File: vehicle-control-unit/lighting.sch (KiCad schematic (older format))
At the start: 23 parts, among them J12 Conn_01x06_Male, Q1 BC517, U3 ULN2803A

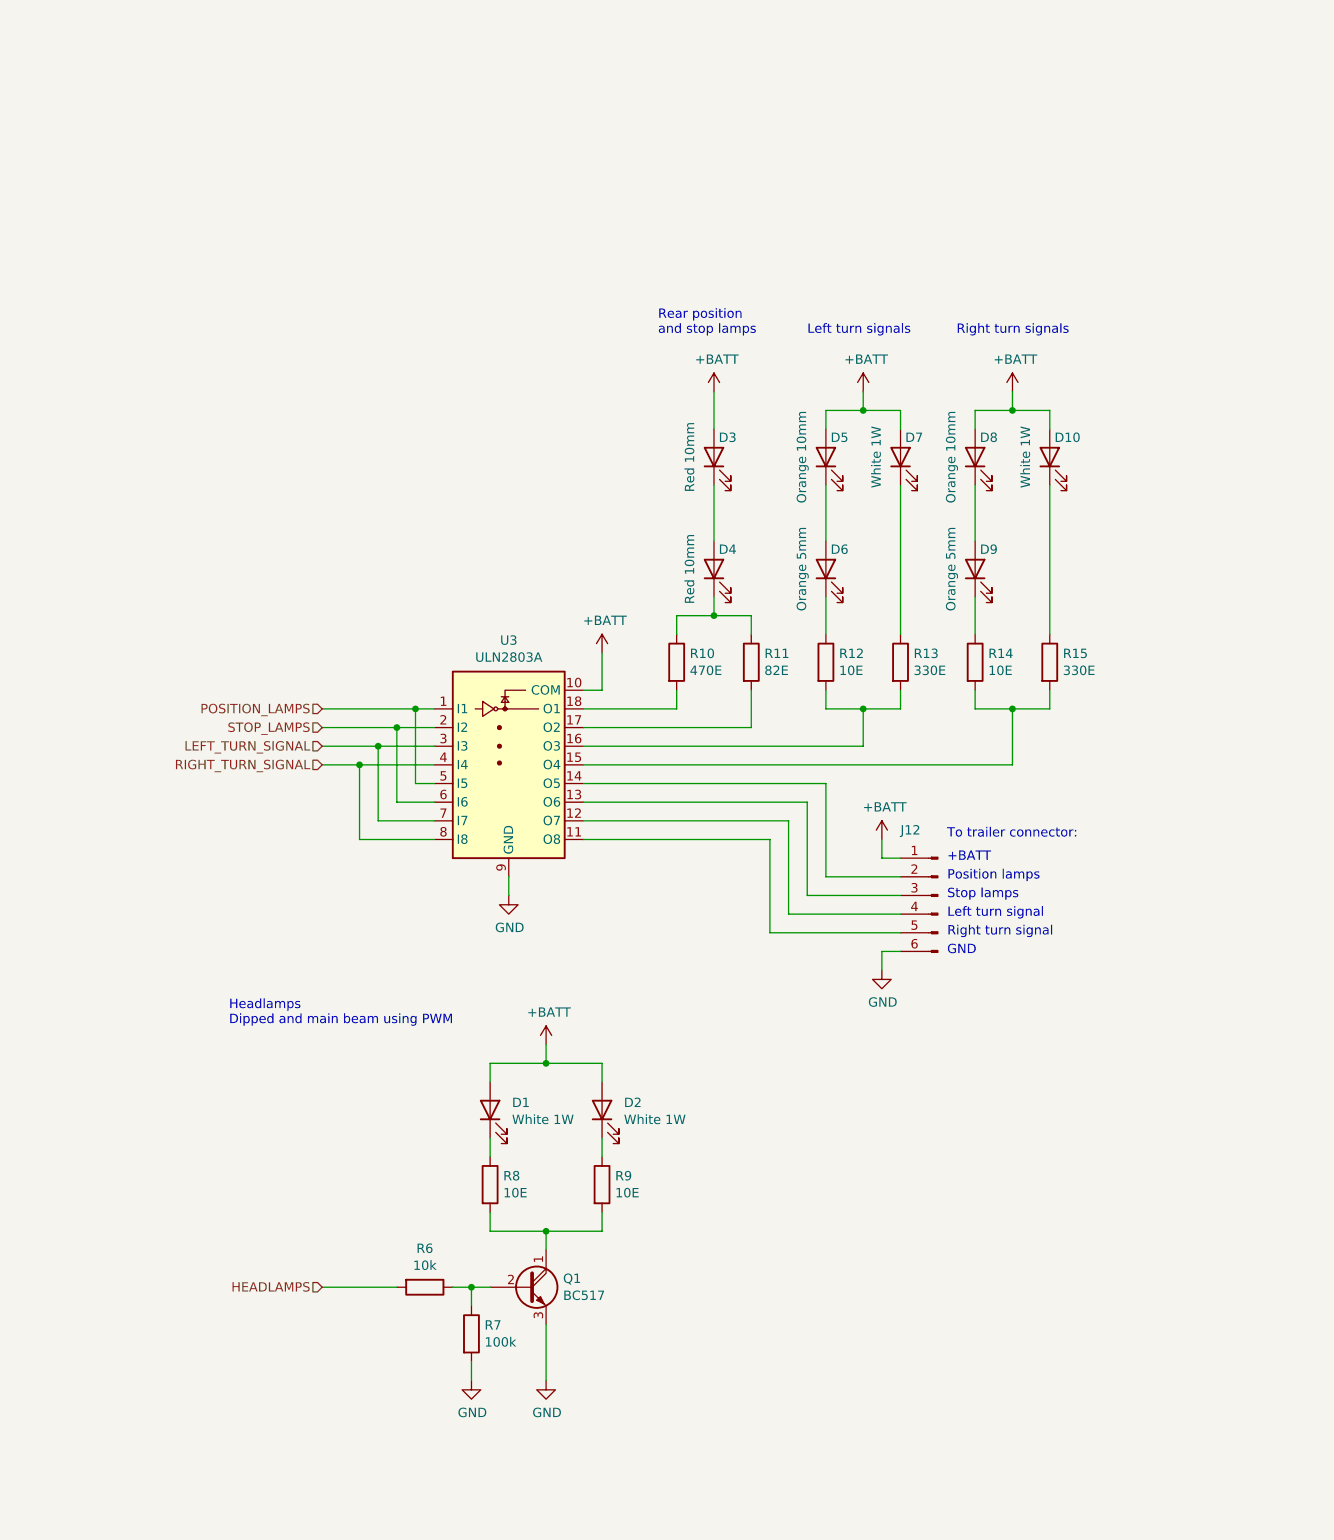
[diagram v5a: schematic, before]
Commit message: Wire all turn signal LEDs in parallel
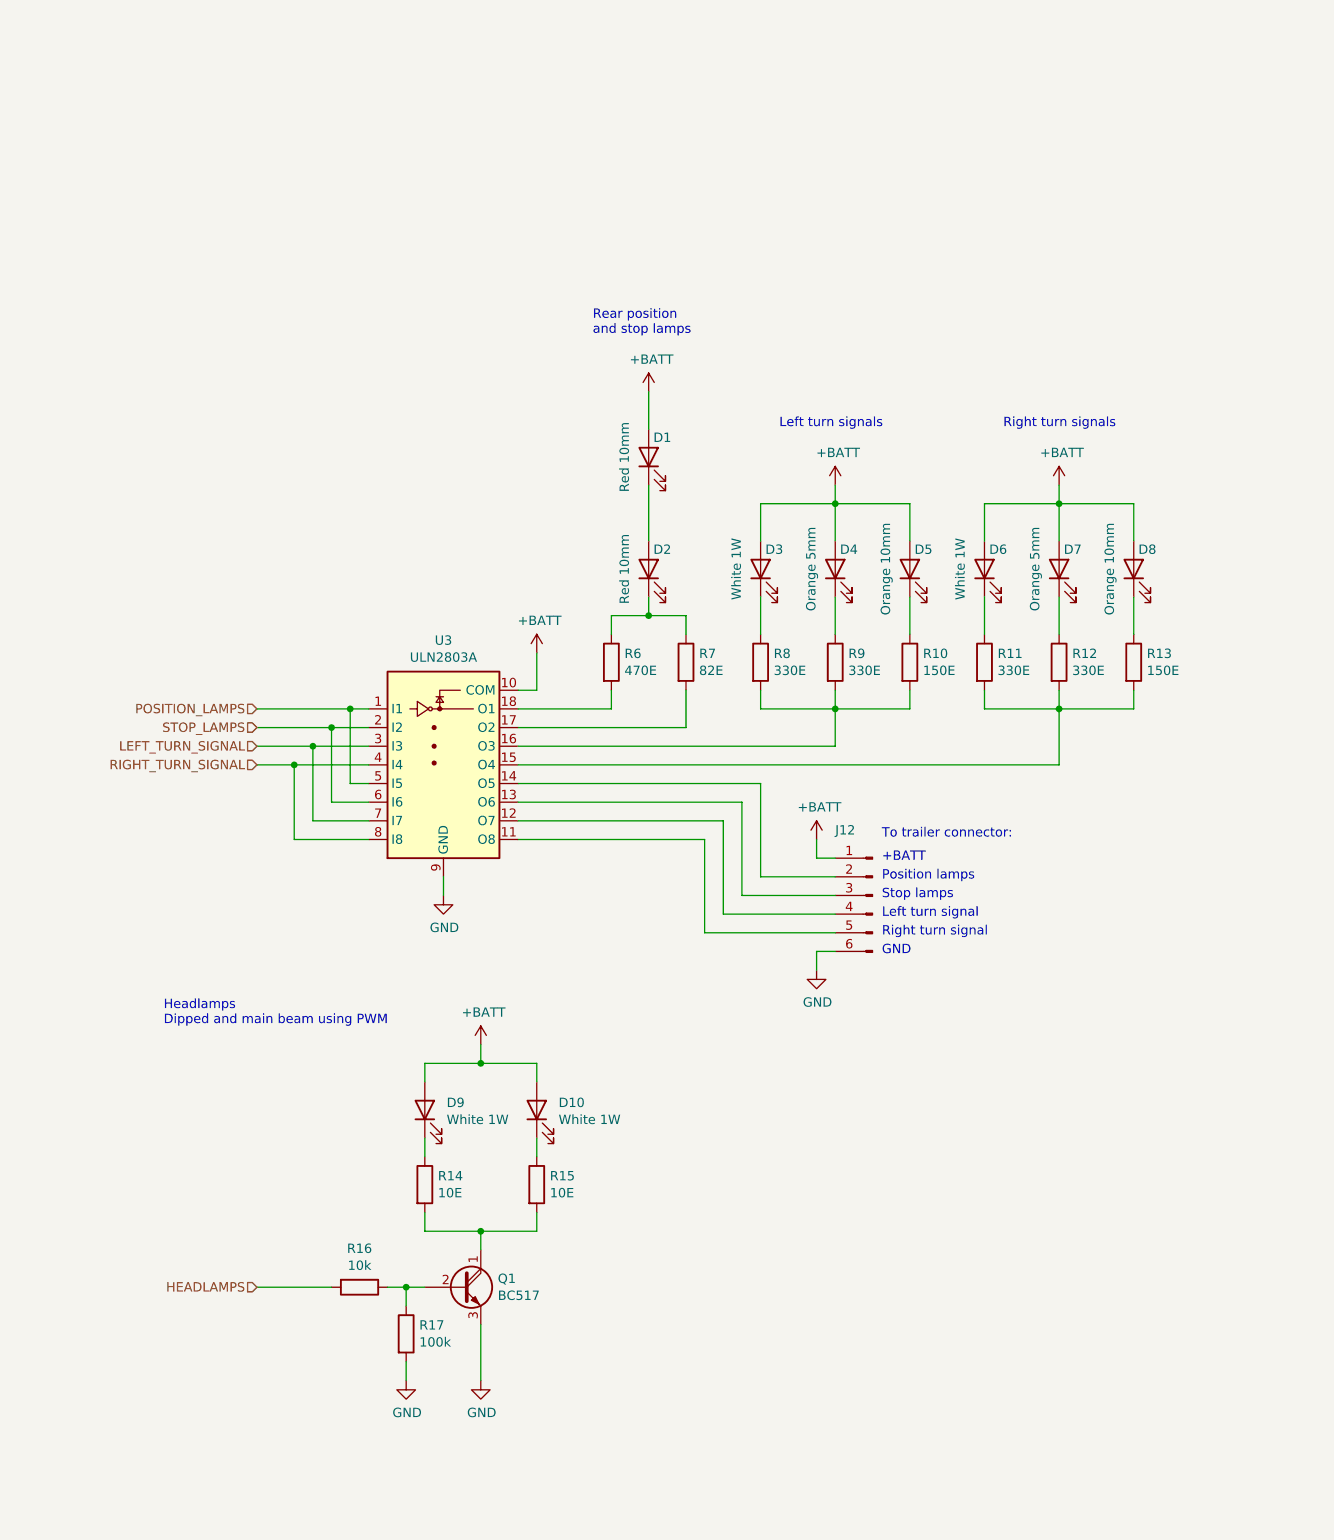
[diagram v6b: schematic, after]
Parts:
- added R10, R13: 150E, symbol Device:R
- R11: renamed from R14; value 10E -> 330E
- R8: renamed from R12; value 10E -> 330E
- renumbered D3 to D1, D2 to D10, D4 to D2, D7 to D3, D6 to D4, D10 to D6, D9 to D7, D1 to D9, R15 to R12, R8 to R14, R9 to R15, R6 to R16, R7 to R17, R10 to R6, R11 to R7, R13 to R9
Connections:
- net +BATT: now also D4.2 (A), D7.2 (A)
- net at R11.2, R12.2, U3.15 (O4): now also R13.2
- net at R8.2, R9.2, U3.16 (O3): now also R10.2
- net at D5.1 (K): now also R10.1; no longer D4.2 (A)
- net at D4.1 (K): now also R9.1; no longer R8.1
- net at D3.1 (K): now also R8.1; no longer R9.1
- net at D8.1 (K): now also R13.1; no longer D7.2 (A)
- net at D7.1 (K): now also R12.1; no longer R11.1
- net at D6.1 (K): now also R11.1; no longer R12.1
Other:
- moved on the sheet: D1, D10, D2, D3, D4, D5, D6, D7, D8, D9, J12, Q1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

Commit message: Assign footprints
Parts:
- D1, D10, D2, D3, D4, D5, D6, D7, D8, D9: footprint (none) -> Connector_PinHeader_2.54mm:PinHeader_1x02_P2.54mm_Horizontal
- J12: footprint (none) -> Connector_PinHeader_2.54mm:PinHeader_1x06_P2.54mm_Horizontal
- R10, R11, R12, R13, R14, R15, R16, R17, R6, R7, R8, R9: footprint (none) -> Resistor_THT:R_Axial_DIN0207_L6.3mm_D2.5mm_P10.16mm_Horizontal
- U3: footprint (none) -> Package_DIP:DIP-18_W7.62mm
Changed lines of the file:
@@
 F 0 "R17" H 3120 8746 50  0000 L CNN
 F 1 "100k" H 3120 8655 50  0000 L CNN
-F 2 "" V 2980 8700 50  0001 C CNN
+F 2 "Resistor_THT:R_Axial_DIN0207_L6.3mm_D2.5mm_P10.16mm_Horizontal" V 2980 8700 50  0001 C CNN
 F 3 "~" H 3050 8700 50  0001 C CNN
 	1    3050 8700
@@
 F 0 "R16" V 2593 8450 50  0000 C CNN
 F 1 "10k" V 2684 8450 50  0000 C CNN
-F 2 "" V 2730 8450 50  0001 C CNN
+F 2 "Resistor_THT:R_Axial_DIN0207_L6.3mm_D2.5mm_P10.16mm_Horizontal" V 2730 8450 50  0001 C CNN
 F 3 "~" H 2800 8450 50  0001 C CNN
 	1    2800 8450
@@
 F 0 "R14" H 3220 7946 50  0000 L CNN
 F 1 "10E" H 3220 7855 50  0000 L CNN
-F 2 "" V 3080 7900 50  0001 C CNN
+F 2 "Resistor_THT:R_Axial_DIN0207_L6.3mm_D2.5mm_P10.16mm_Horizontal" V 3080 7900 50  0001 C CNN
 F 3 "~" H 3150 7900 50  0001 C CNN
 	1    3150 7900
@@
 F 0 "R15" H 3820 7946 50  0000 L CNN
 F 1 "10E" H 3820 7855 50  0000 L CNN
-F 2 "" V 3680 7900 50  0001 C CNN
+F 2 "Resistor_THT:R_Axial_DIN0207_L6.3mm_D2.5mm_P10.16mm_Horizontal" V 3680 7900 50  0001 C CNN
 F 3 "~" H 3750 7900 50  0001 C CNN
 	1    3750 7900
@@
 F 0 "D9" V 3189 7383 50  0000 R CNN
 F 1 "White 1W" V 3098 7383 50  0000 R CNN
-F 2 "" H 3150 7500 50  0001 C CNN
+F 2 "Connector_PinHeader_2.54mm:PinHeader_1x02_P2.54mm_Horizontal" H 3150 7500 50  0001 C CNN
 F 3 "~" H 3150 7500 50  0001 C CNN
 	1    3150 7500
@@
 F 0 "D10" V 3789 7383 50  0000 R CNN
 F 1 "White 1W" V 3698 7383 50  0000 R CNN
-F 2 "" H 3750 7500 50  0001 C CNN
+F 2 "Connector_PinHeader_2.54mm:PinHeader_1x02_P2.54mm_Horizontal" H 3750 7500 50  0001 C CNN
 F 3 "~" H 3750 7500 50  0001 C CNN
 	1    3750 7500
@@
 F 0 "R8" H 5020 5146 50  0000 L CNN
 F 1 "330E" H 5020 5055 50  0000 L CNN
-F 2 "" V 4880 5100 50  0001 C CNN
+F 2 "Resistor_THT:R_Axial_DIN0207_L6.3mm_D2.5mm_P10.16mm_Horizontal" V 4880 5100 50  0001 C CNN
 F 3 "~" H 4950 5100 50  0001 C CNN
 	1    4950 5100
@@
 F 0 "R11" H 6220 5146 50  0000 L CNN
 F 1 "330E" H 6220 5055 50  0000 L CNN
-F 2 "" V 6080 5100 50  0001 C CNN
+F 2 "Resistor_THT:R_Axial_DIN0207_L6.3mm_D2.5mm_P10.16mm_Horizontal" V 6080 5100 50  0001 C CNN
 F 3 "~" H 6150 5100 50  0001 C CNN
 	1    6150 5100
@@
 F 0 "D7" V 6625 4575 50  0000 R TNN
 F 1 "Orange 5mm" H 6550 4700 50  0000 C BNN
-F 2 "" H 6550 4600 50  0001 C CNN
+F 2 "Connector_PinHeader_2.54mm:PinHeader_1x02_P2.54mm_Horizontal" H 6550 4600 50  0001 C CNN
 F 3 "~" H 6550 4600 50  0001 C CNN
 	1    6550 4600
@@
 F 0 "D6" V 6225 4575 50  0000 R TNN
 F 1 "White 1W" H 6150 4700 50  0000 C BNN
-F 2 "" H 6150 4600 50  0001 C CNN
+F 2 "Connector_PinHeader_2.54mm:PinHeader_1x02_P2.54mm_Horizontal" H 6150 4600 50  0001 C CNN
 F 3 "~" H 6150 4600 50  0001 C CNN
 	1    6150 4600
@@
 F 0 "D3" V 5025 4575 50  0000 R TNN
 F 1 "White 1W" H 4950 4700 50  0000 C BNN
-F 2 "" H 4950 4600 50  0001 C CNN
+F 2 "Connector_PinHeader_2.54mm:PinHeader_1x02_P2.54mm_Horizontal" H 4950 4600 50  0001 C CNN
 F 3 "~" H 4950 4600 50  0001 C CNN
 	1    4950 4600
@@
 F 0 "D4" V 5425 4575 50  0000 R TNN
 F 1 "Orange 5mm" H 5350 4700 50  0000 C BNN
-F 2 "" H 5350 4600 50  0001 C CNN
+F 2 "Connector_PinHeader_2.54mm:PinHeader_1x02_P2.54mm_Horizontal" H 5350 4600 50  0001 C CNN
 F 3 "~" H 5350 4600 50  0001 C CNN
 	1    5350 4600
@@
 F 0 "D5" V 5825 4575 50  0000 R TNN
 F 1 "Orange 10mm" H 5750 4700 50  0000 C BNN
-F 2 "" H 5750 4600 50  0001 C CNN
+F 2 "Connector_PinHeader_2.54mm:PinHeader_1x02_P2.54mm_Horizontal" H 5750 4600 50  0001 C CNN
 F 3 "~" H 5750 4600 50  0001 C CNN
 	1    5750 4600
@@
 F 0 "D8" V 7025 4575 50  0000 R TNN
 F 1 "Orange 10mm" H 6950 4700 50  0000 C BNN
-F 2 "" H 6950 4600 50  0001 C CNN
+F 2 "Connector_PinHeader_2.54mm:PinHeader_1x02_P2.54mm_Horizontal" H 6950 4600 50  0001 C CNN
 F 3 "~" H 6950 4600 50  0001 C CNN
 	1    6950 4600
@@
 F 0 "R10" H 5820 5146 50  0000 L CNN
 F 1 "150E" H 5820 5055 50  0000 L CNN
-F 2 "" V 5680 5100 50  0001 C CNN
+F 2 "Resistor_THT:R_Axial_DIN0207_L6.3mm_D2.5mm_P10.16mm_Horizontal" V 5680 5100 50  0001 C CNN
 F 3 "~" H 5750 5100 50  0001 C CNN
 	1    5750 5100
@@
 F 0 "R13" H 7020 5146 50  0000 L CNN
 F 1 "150E" H 7020 5055 50  0000 L CNN
-F 2 "" V 6880 5100 50  0001 C CNN
+F 2 "Resistor_THT:R_Axial_DIN0207_L6.3mm_D2.5mm_P10.16mm_Horizontal" V 6880 5100 50  0001 C CNN
 F 3 "~" H 6950 5100 50  0001 C CNN
 	1    6950 5100
@@
 F 0 "R6" H 4220 5146 50  0000 L CNN
 F 1 "470E" H 4220 5055 50  0000 L CNN
-F 2 "" V 4080 5100 50  0001 C CNN
+F 2 "Resistor_THT:R_Axial_DIN0207_L6.3mm_D2.5mm_P10.16mm_Horizontal" V 4080 5100 50  0001 C CNN
 F 3 "~" H 4150 5100 50  0001 C CNN
 	1    4150 5100
@@
 F 0 "R7" H 4620 5146 50  0000 L CNN
 F 1 "82E" H 4620 5055 50  0000 L CNN
-F 2 "" V 4480 5100 50  0001 C CNN
+F 2 "Resistor_THT:R_Axial_DIN0207_L6.3mm_D2.5mm_P10.16mm_Horizontal" V 4480 5100 50  0001 C CNN
 F 3 "~" H 4550 5100 50  0001 C CNN
 	1    4550 5100
@@
 F 0 "R9" H 5420 5146 50  0000 L CNN
 F 1 "330E" H 5420 5055 50  0000 L CNN
-F 2 "" V 5280 5100 50  0001 C CNN
+F 2 "Resistor_THT:R_Axial_DIN0207_L6.3mm_D2.5mm_P10.16mm_Horizontal" V 5280 5100 50  0001 C CNN
 F 3 "~" H 5350 5100 50  0001 C CNN
 	1    5350 5100
@@
 F 0 "R12" H 6620 5146 50  0000 L CNN
 F 1 "330E" H 6620 5055 50  0000 L CNN
-F 2 "" V 6480 5100 50  0001 C CNN
+F 2 "Resistor_THT:R_Axial_DIN0207_L6.3mm_D2.5mm_P10.16mm_Horizontal" V 6480 5100 50  0001 C CNN
 F 3 "~" H 6550 5100 50  0001 C CNN
 	1    6550 5100
@@
 F 0 "D1" V 4425 3975 50  0000 R TNN
 F 1 "Red 10mm" H 4350 4100 50  0000 C BNN
-F 2 "" H 4350 4000 50  0001 C CNN
+F 2 "Connector_PinHeader_2.54mm:PinHeader_1x02_P2.54mm_Horizontal" H 4350 4000 50  0001 C CNN
 F 3 "~" H 4350 4000 50  0001 C CNN
 	1    4350 4000
@@
 F 0 "D2" V 4425 4575 50  0000 R TNN
 F 1 "Red 10mm" H 4350 4700 50  0000 C BNN
-F 2 "" H 4350 4600 50  0001 C CNN
+F 2 "Connector_PinHeader_2.54mm:PinHeader_1x02_P2.54mm_Horizontal" H 4350 4600 50  0001 C CNN
 F 3 "~" H 4350 4600 50  0001 C CNN
 	1    4350 4600
@@
 F 0 "J12" H 5750 6700 50  0000 R CNN
 F 1 "Conn_01x06_Male" H 5522 6233 50  0001 R CNN
-F 2 "" H 5550 6350 50  0001 C CNN
+F 2 "Connector_PinHeader_2.54mm:PinHeader_1x06_P2.54mm_Horizontal" H 5550 6350 50  0001 C CNN
 F 3 "~" H 5550 6350 50  0001 C CNN
 	1    5550 6350
@@
 F 0 "U3" H 3250 6117 50  0000 C CNN
 F 1 "ULN2803A" H 3250 6026 50  0000 C CNN
-F 2 "" H 3300 4900 50  0001 L CNN
+F 2 "Package_DIP:DIP-18_W7.62mm" H 3300 4900 50  0001 L CNN
 F 3 "http://www.ti.com/lit/ds/symlink/uln2803a.pdf" H 3350 5350 50  0001 C CNN
 	1    3250 5550

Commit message: Route PCB
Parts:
- removed D1, D2: Red 10mm, Connector_PinHeader_2.54mm:PinHeader_1x02_P2.54mm_Horizontal, symbol Device:LED
- removed D10, D3, D6, D9: White 1W, Connector_PinHeader_2.54mm:PinHeader_1x02_P2.54mm_Horizontal, symbol Device:LED
- removed D4, D7: Orange 5mm, Connector_PinHeader_2.54mm:PinHeader_1x02_P2.54mm_Horizontal, symbol Device:LED
- removed D5, D8: Orange 10mm, Connector_PinHeader_2.54mm:PinHeader_1x02_P2.54mm_Horizontal, symbol Device:LED
- removed J12: Conn_01x06_Male, Connector_PinHeader_2.54mm:PinHeader_1x06_P2.54mm_Horizontal, symbol Connector:Conn_01x06_Male
- added J7, J8: Conn_01x03_Male, Connector_PinHeader_2.54mm:PinHeader_1x03_P2.54mm_Horizontal, symbol Connector:Conn_01x03_Male
- added J9: Conn_02x06_Male_UnitPerRow, Connector_PinHeader_2.54mm:PinHeader_2x06_P2.54mm_Horizontal, symbol earth-rover-symbols:Conn_02x06_Male_UnitPerRow
- renumbered R8 to R10, R6 to R11, R10 to R12, R11 to R14, R7 to R15, R9 to R16, R12 to R17, R14 to R6, R15 to R7, R16 to R8, R17 to R9
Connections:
- net +BATT: now also J7.1 (Pin_1), J8.1 (Pin_1), J9.1 (Pin_1), J9.2 (Pin_2)
- net GND: now also J9.11 (Pin_11)
- net LEFT_TURN_SIGNAL: now also U3.5 (I5), U3.6 (I6); no longer U3.3 (I3), U3.7 (I7)
- net POSITION_LAMPS: now also U3.2 (I2); no longer U3.5 (I5)
- net RIGHT_TURN_SIGNAL: now also U3.7 (I7); no longer U3.4 (I4)
- net STOP_LAMPS: now also U3.3 (I3), U3.4 (I4); no longer U3.2 (I2), U3.6 (I6)
- net at U3.11 (O8): now also J9.9 (Pin_9)
- net at U3.12 (O7): now also R13.2, R14.2, R17.2
- net at U3.13 (O6): now also J9.7 (Pin_7)
- net at U3.14 (O5): now also R10.2, R12.2, R16.2
- net at R15.2: now also U3.16 (O3); no longer U3.17 (O2)
- net at R6.1: now also J7.2 (Pin_2)
- net at R7.1: now also J8.2 (Pin_2)
- net at R11.1, R15.1: now also J9.4 (Pin_4)
- net at R12.1: now also J9.6 (Pin_6)
- net at R16.1: now also J9.8 (Pin_8)
- net at R10.1: now also J7.3 (Pin_3)
- net at R13.1: now also J9.10 (Pin_10)
- net at R17.1: now also J9.12 (Pin_12)
- net at R14.1: now also J8.3 (Pin_3)
- new net: J9.5 (Pin_5), U3.15 (O4)
- new net: J9.3 (Pin_3), U3.17 (O2)
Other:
- note added: "Left front turn signal (1W white LED) sink"
- note added: "Left headlamp (1W white LED) sink"
- note added: "Left rear turn signal (10mm orange LED) sink"
- note added: "Left side turn signal (5mm orange LED) sink"
- note added: "Left turn signal sink"
- note added: "Position lamps (2 * 10mm red LED) sink"
- note added: "Position lamps sink"
- note added: "Right front turn signal (1W white LED) sink"
- note added: "Right headlamp (1W white LED) sink"
- note added: "Right rear turn signal (10mm orange LED) sink"
- note added: "Right side turn signal (5mm orange LED) sink"
- note added: "Right turn signal sink"
- note added: "Stop lamps sink"
- note added: "To front left lamps:"
- note added: "To front right lamps:"
- note added: "To rear lamps:"
- note added: "To trailer connector\n(resistors in trailer):"
- note removed: "Headlamps\nDipped and main beam using PWM"
- note removed: "Left turn signal"
- note removed: "Left turn signals"
- note removed: "Position lamps"
- note removed: "Rear position\nand stop lamps"
- note removed: "Right turn signal"
- note removed: "Right turn signals"
- note removed: "Stop lamps"
- note removed: "To trailer connector:"
- moved on the sheet: Q1, R10, R11, R12, R13, R14, R15, R16, R17, R6, R7, R8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
